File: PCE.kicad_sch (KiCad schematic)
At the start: 1 part, among them J1 4P2C

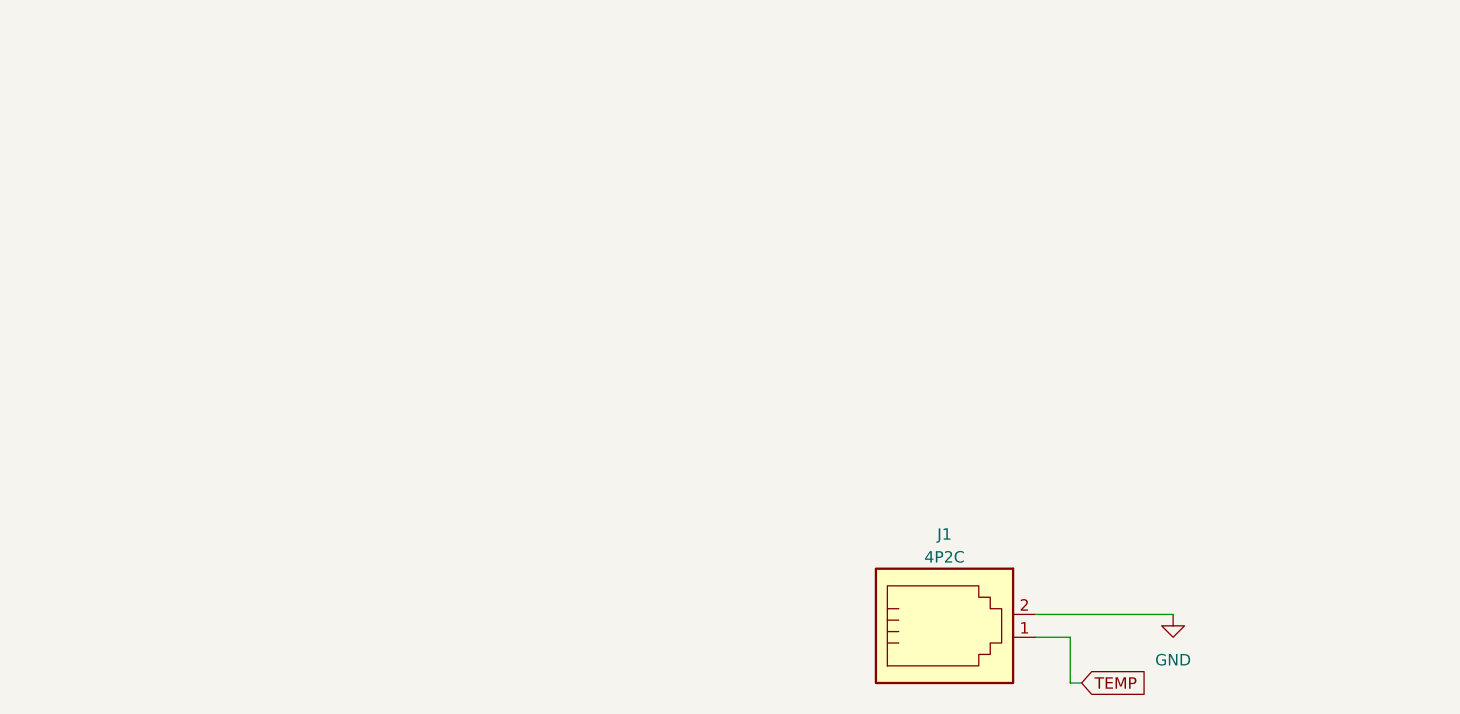
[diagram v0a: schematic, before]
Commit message: Import TG16 schematics and update PCB.
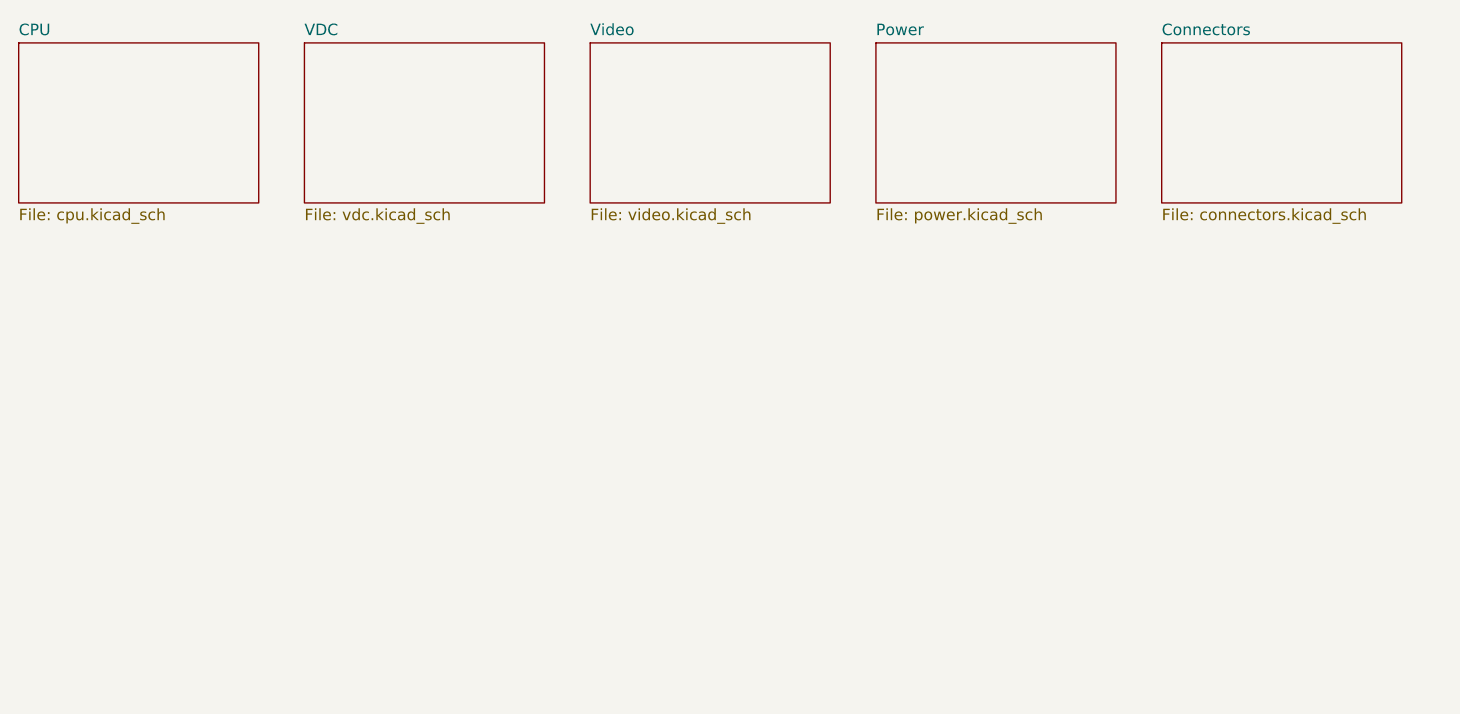
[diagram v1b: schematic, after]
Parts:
- removed J1: 4P2C, symbol Connector:4P2C
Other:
- added sheet CPU (cpu.kicad_sch)
- added sheet Connectors (connectors.kicad_sch)
- added sheet Power (power.kicad_sch)
- added sheet VDC (vdc.kicad_sch)
- added sheet Video (video.kicad_sch)
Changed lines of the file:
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@@
 (kicad_sch (version 20230121) (generator eeschema)
-  (paper "A4")
-  (wire (pts (xy 153.67 106.68) (xy 154.94 106.68))
-    (stroke (width 0) (type default))
-  )
-  (wire (pts (xy 149.86 101.6) (xy 153.67 101.6))
-    (stroke (width 0) (type default))
-  )
-  (wire (pts (xy 153.67 101.6) (xy 153.67 106.68))
-    (stroke (width 0) (type default))
-  )
-  (wire (pts (xy 149.86 99.06) (xy 165.1 99.06))
-    (stroke (width 0) (type default))
-  )
-  (global_label "TEMP" (shape input) (at 154.94 106.68 0) (fields_autoplaced)
-    (effects (font (size 1.27 1.27)) (justify left))
-    (property "Intersheetrefs" "${INTERSHEET_REFS}" (at 162.6838 106.68 0)
-      (effects (font (size 1.27 1.27)) (justify left) hide)
+  (paper "A3")
+  (sheet (at 36.83 35.56) (size 26.67 17.78) (fields_autoplaced)
+    (stroke (width 0.1524) (type solid))
+    (fill (color 0 0 0 0.0000))
+    (property "Sheetname" "CPU" (at 36.83 34.8484 0)
+      (effects (font (size 1.27 1.27)) (justify left bottom))
     )
-  )
-  (symbol (lib_id "Connector:4P2C") (at 139.7 101.6 0) (unit 1)
-    (in_bom yes) (on_board yes) (dnp no) (fields_autoplaced)
-    (property "Reference" "J1" (at 139.7 90.17 0)
-      (effects (font (size 1.27 1.27)))
+    (property "Sheetfile" "cpu.kicad_sch" (at 36.83 53.9246 0)
+      (effects (font (size 1.27 1.27)) (justify left top))
     )
-    (property "Value" "4P2C" (at 139.7 92.71 0)
-      (effects (font (size 1.27 1.27)))
-    )
-    (property "Footprint" "" (at 139.7 100.33 90)
-      (effects (font (size 1.27 1.27)) hide)
-    )
-    (property "Datasheet" "~" (at 139.7 100.33 90)
-      (effects (font (size 1.27 1.27)) hide)
-    )
-    (pin "1")
-    (pin "2")
     (instances
       (project "PCE"
-        (path "/c1cb2bef-9eae-4ec7-9810-1daf2061cc41"
-          (reference "J1") (unit 1)
-        )
+        (path "/c1c718c6-a427-431e-a18b-e46f94ae8e09" (page "1"))
       )
     )
   )
-  (symbol (lib_id "power:GND") (at 165.1 99.06 0) (unit 1)
-    (in_bom yes) (on_board yes) (dnp no) (fields_autoplaced)
-    (property "Reference" "#PWR01" (at 165.1 105.41 0)
-      (effects (font (size 1.27 1.27)) hide)
+  (sheet (at 163.83 35.56) (size 26.67 17.78) (fields_autoplaced)
+    (stroke (width 0.1524) (type solid))
+    (fill (color 0 0 0 0.0000))
+    (property "Sheetname" "Connectors" (at 163.83 34.8484 0)
+      (effects (font (size 1.27 1.27)) (justify left bottom))
     )
-    (property "Value" "GND" (at 165.1 104.14 0)
-      (effects (font (size 1.27 1.27)))
+    (property "Sheetfile" "connectors.kicad_sch" (at 163.83 53.9246 0)
+      (effects (font (size 1.27 1.27)) (justify left top))
     )
-    (property "Footprint" "" (at 165.1 99.06 0)
-      (effects (font (size 1.27 1.27)) hide)
-    )
-    (property "Datasheet" "" (at 165.1 99.06 0)
-      (effects (font (size 1.27 1.27)) hide)
-    )
-    (pin "1")
     (instances
       (project "PCE"
-        (path "/c1cb2bef-9eae-4ec7-9810-1daf2061cc41"
-          (reference "#PWR01") (unit 1)
-        )
+        (path "/c1c718c6-a427-431e-a18b-e46f94ae8e09" (page "5"))
+      )
+    )
+  )
+  (sheet (at 132.08 35.56) (size 26.67 17.78) (fields_autoplaced)
+    (stroke (width 0.1524) (type solid))
+    (fill (color 0 0 0 0.0000))
+    (property "Sheetname" "Power" (at 132.08 34.8484 0)
+      (effects (font (size 1.27 1.27)) (justify left bottom))
+    )
+    (property "Sheetfile" "power.kicad_sch" (at 132.08 53.9246 0)
+      (effects (font (size 1.27 1.27)) (justify left top))
+    )
+    (instances
+      (project "PCE"
+        (path "/c1c718c6-a427-431e-a18b-e46f94ae8e09" (page "4"))
+      )
+    )
+  )
+  (sheet (at 100.33 35.56) (size 26.67 17.78) (fields_autoplaced)
+    (stroke (width 0.1524) (type solid))
+    (fill (color 0 0 0 0.0000))
+    (property "Sheetname" "Video" (at 100.33 34.8484 0)
+      (effects (font (size 1.27 1.27)) (justify left bottom))
+    )
+    (property "Sheetfile" "video.kicad_sch" (at 100.33 53.9246 0)
+      (effects (font (size 1.27 1.27)) (justify left top))
+    )
+    (instances
+      (project "PCE"
+        (path "/c1c718c6-a427-431e-a18b-e46f94ae8e09" (page "3"))
+      )
+    )
+  )
+  (sheet (at 68.58 35.56) (size 26.67 17.78) (fields_autoplaced)
+    (stroke (width 0.1524) (type solid))
+    (fill (color 0 0 0 0.0000))
+    (property "Sheetname" "VDC" (at 68.58 34.8484 0)
+      (effects (font (size 1.27 1.27)) (justify left bottom))
+    )
+    (property "Sheetfile" "vdc.kicad_sch" (at 68.58 53.9246 0)
+      (effects (font (size 1.27 1.27)) (justify left top))
+    )
+    (instances
+      (project "PCE"
+        (path "/c1c718c6-a427-431e-a18b-e46f94ae8e09" (page "2"))
       )
     )
   )
   (sheet_instances
-    (path "/" (page "1"))
+    (path "/" (page "6"))
   )
 )

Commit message: Silkscreen stuff, tidy schematics, corrections.
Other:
- title: (none) -> Index
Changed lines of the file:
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@@
 (kicad_sch (version 20230121) (generator eeschema)
   (paper "A3")
+  (title_block
+    (title "Index")
+    (date "2023-08-17")
+    (rev "1.0")
+    (comment 1 "Differences reverse engineered from original PWD-623A board")
+    (comment 2 "Adapted from existing TurboGrafx-16 schematics by Cosam")
+  )
   (sheet (at 36.83 35.56) (size 26.67 17.78) (fields_autoplaced)
     (stroke (width 0.1524) (type solid))
